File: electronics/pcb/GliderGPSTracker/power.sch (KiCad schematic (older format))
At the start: 28 parts

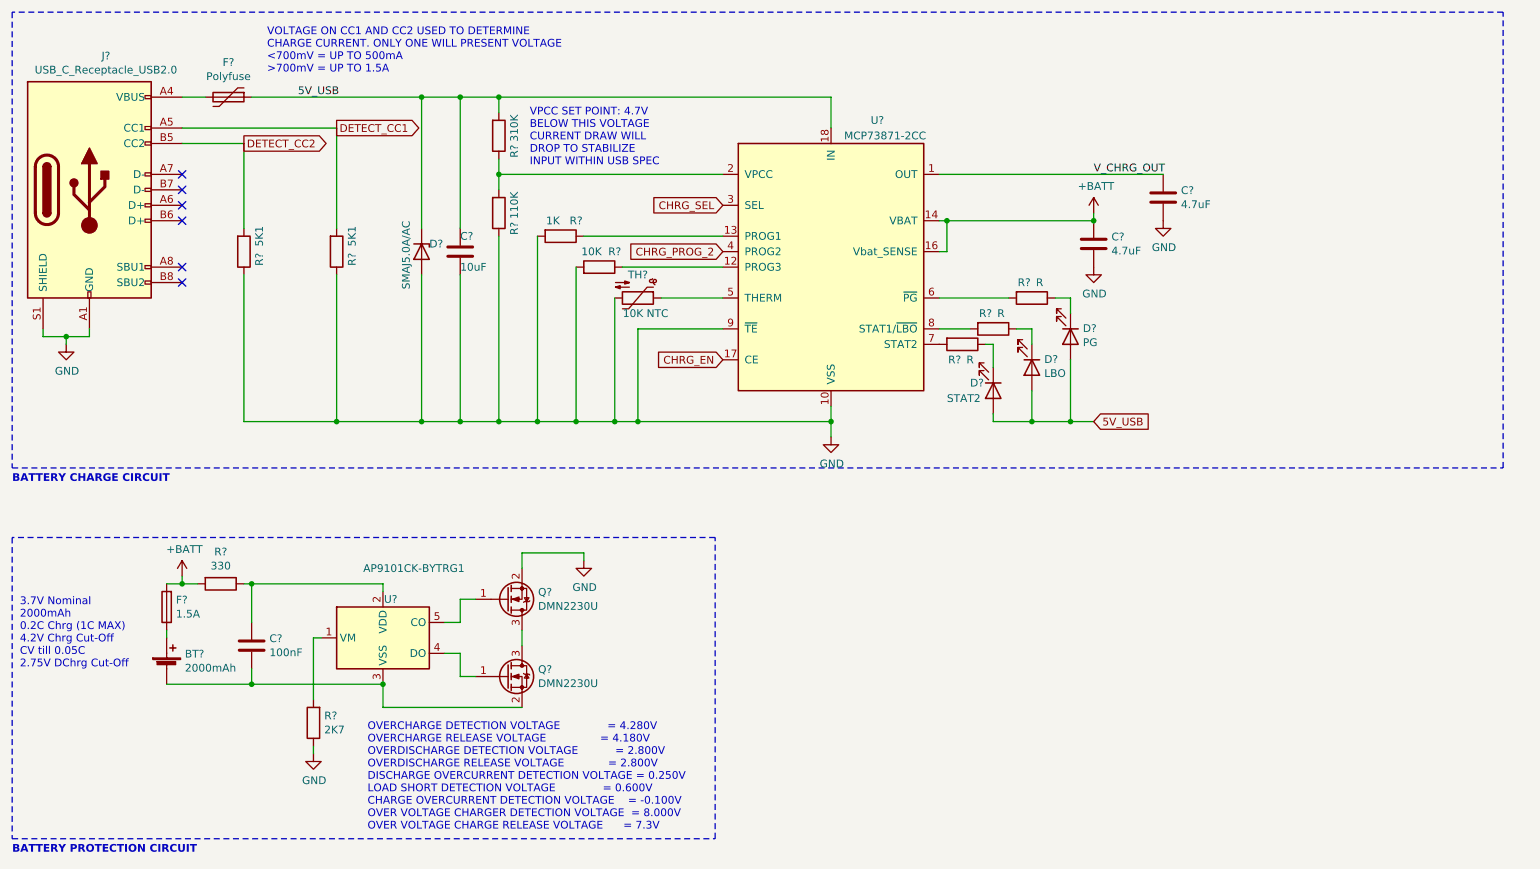
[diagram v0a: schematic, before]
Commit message: Task: Begin SIM7000E implementation
Work has begun on adding the SIM7000E module to the schematic.
A schematic symbol and footprint have been made to this end.
The basic SIM card circuit and power circuit has been set up
which include ESD protection IC's.
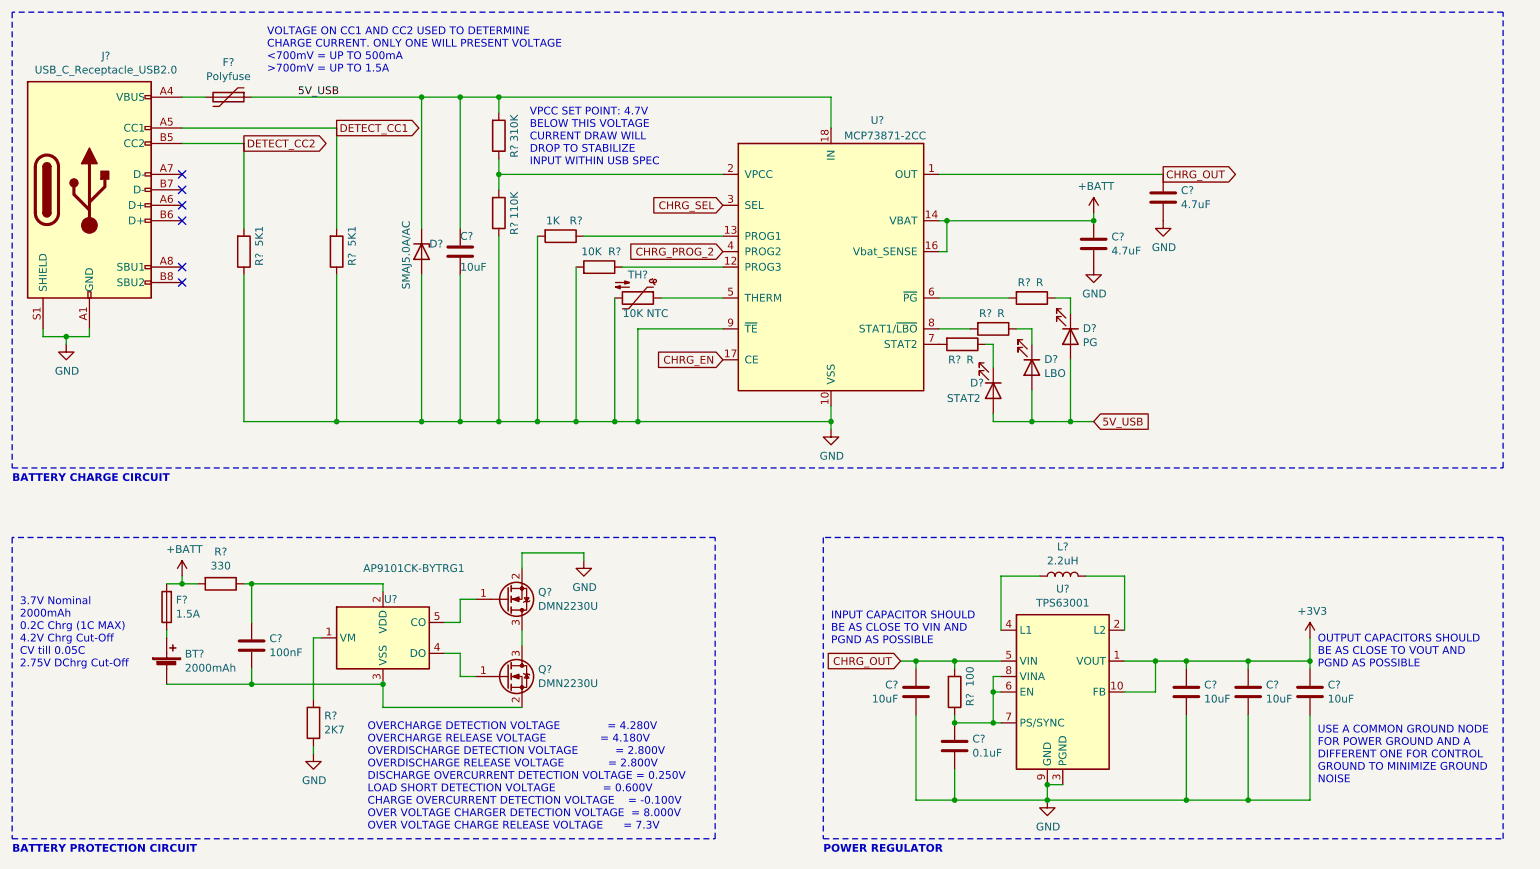
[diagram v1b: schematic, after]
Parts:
- added C? (x4): 10uF, symbol Device:C
- added C?: 0.1uF, symbol Device:C
- added L?: 2.2uH, symbol Device:L
- added R?: 100, symbol Device:R
- added U?: TPS63001, Package_SON:Texas_DRC0010J_ThermalVias, symbol Regulator_Switching:TPS63001
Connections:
- net GND: now also C?.2, C?.2, C?.2, C?.2, C?.2, U?.11 (PGND), U?.3 (PGND), U?.9 (GND)
- net V_CHRG_OUT renamed CHRG_OUT
- net CHRG_OUT: now also C?.1, R?.2, U?.5 (VIN)
- new net: L?.2, U?.2 (L2)
- new net: L?.1, U?.4 (L1)
- new net: C?.1, R?.1, U?.6 (EN), U?.7 (PS/SYNC), U?.8 (VINA)
- new net +3V3: C?.1, C?.1, C?.1, U?.1 (VOUT), U?.10 (FB)
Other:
- note added: "INPUT CAPACITOR SHOULD\nBE AS CLOSE TO VIN AND \nPGND AS POSSIBLE"
- note added: "OUTPUT CAPACITORS SHOULD\nBE AS CLOSE TO VOUT AND \nPGND AS POSSIBLE"
- note added: "POWER REGULATOR"
- note added: "USE A COMMON GROUND NODE\nFOR POWER GROUND AND A \nDIFFERENT ONE FOR CONTROL\nGROUND TO MINIMIZE GROUND\nNOISE"

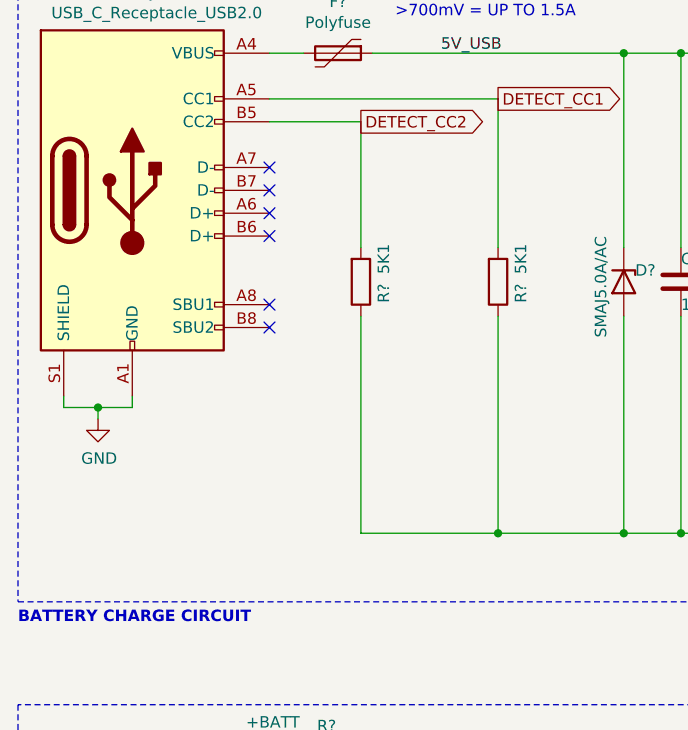
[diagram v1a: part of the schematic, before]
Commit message: Task: SIM7000 Powerkey, reset, USB, UART implementation
The SIM7000 schematic has been updated to include the recommended
layouts for the Powerkey pin, reset pin, USB and UART buses, and
netlight pin. The usb connector in the power schematic has also
been updated to accomodate the additions.
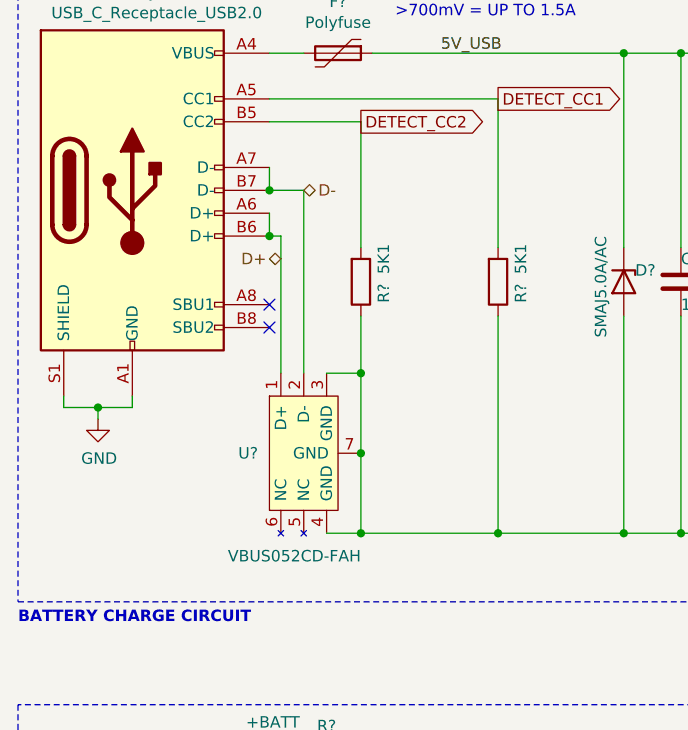
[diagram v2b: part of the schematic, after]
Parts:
- added U?: VBUS052CD-FAH, symbol GliderGPSLibrary:VBUS052CD-FAH
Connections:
- net GND: now also U?.3 (GND), U?.4 (GND), U?.7 (GND)
- net D+: now reaches J?.A6 (D+)
- net D+: now also J?.B6 (D+), U?.1 (D+)
- net D-: now reaches J?.A7 (D-)
- net D-: now also J?.B7 (D-), U?.2 (D-)
- no-connect marks 6 -> 2
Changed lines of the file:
@@
 $Descr A4 11693 8268
 encoding utf-8
-Sheet 2 3
+Sheet 2 4
 Title "POWER"
 Date ""
@@
 	1    0    0    -1
 $EndComp
-$Comp
-L Device:R R?
-U 1 1 6094CFBA
-P 2450 2400
-AR Path="/6094CFBA" Ref="R?"  Part="1"
-AR Path="/6090E0C9/6094CFBA" Ref="R?"  Part="1"
-F 0 "R?" V 2550 2450 50  0000 C CNN
-F 1 "5K1" V 2550 2300 50  0000 C CNN
-F 2 "" V 2380 2400 50  0001 C CNN
-F 3 "~" H 2450 2400 50  0001 C CNN
-	1    2450 2400
-	1    0    0    1
-$EndComp
 Wire Wire Line
 	2050 1700 2450 1700
-Wire Wire Line
-	2450 1700 2450 2250
-Wire Wire Line
-	2450 2550 2450 3500
-Wire Wire Line
-	2450 3500 3050 3500
 Connection ~ 3050 3500
 Text GLabel 2450 1700 2    50   Output ~ 0
@@
 NoConn ~ 2050 2500
 NoConn ~ 2050 2600
-NoConn ~ 2050 2200
-NoConn ~ 2050 2100
-NoConn ~ 2050 2000
-NoConn ~ 2050 1900
 Text Notes 2600 1250 0    50   ~ 0
 VOLTAGE ON CC1 AND CC2 USED TO DETERMINE\nCHARGE CURRENT. ONLY ONE WILL PRESENT VOLTAGE\n<700mV = UP TO 500mA\n>700mV = UP TO 1.5A
@@
 Text Notes 6200 6300 0    50   ~ 10
 POWER REGULATOR
+Wire Wire Line
+	2050 2100 2050 2200
+Connection ~ 2050 2200
+Wire Wire Line
+	2050 1900 2050 2000
+Connection ~ 2050 2000
+Wire Wire Line
+	2050 2200 2100 2200
+Wire Wire Line
+	2050 2000 2200 2000
+Wire Wire Line
+	2100 2200 2100 2800
+Wire Wire Line
+	2200 2000 2200 2800
+Connection ~ 2450 3500
+Wire Wire Line
+	2300 3500 2450 3500
+Wire Wire Line
+	2450 2800 2450 3150
+Wire Wire Line
+	2300 2800 2450 2800
+Wire Wire Line
+	2450 3150 2450 3500
+Connection ~ 2450 3150
+$Comp
+L GliderGPSLibrary:VBUS052CD-FAH U?
+U 1 1 60CF3EBE
+P 2200 3150
+F 0 "U?" V 2200 3350 50  0000 L CNN
+F 1 "VBUS052CD-FAH" V 2650 2900 50  0000 L CNN
+F 2 "" H 2200 2500 50  0001 C CNN
+F 3 "" H 2200 2500 50  0001 C CNN
+	1    2200 3150
+	0    -1   1    0
+$EndComp
+Wire Wire Line
+	2450 3500 3050 3500
+Connection ~ 2450 2800
+Wire Wire Line
+	2450 2550 2450 2800
+Wire Wire Line
+	2450 1700 2450 2250
+$Comp
+L Device:R R?
+U 1 1 6094CFBA
+P 2450 2400
+AR Path="/6094CFBA" Ref="R?"  Part="1"
+AR Path="/6090E0C9/6094CFBA" Ref="R?"  Part="1"
+F 0 "R?" V 2550 2450 50  0000 C CNN
+F 1 "5K1" V 2550 2300 50  0000 C CNN
+F 2 "" V 2380 2400 50  0001 C CNN
+F 3 "~" H 2450 2400 50  0001 C CNN
+	1    2450 2400
+	1    0    0    1
+$EndComp
+Text HLabel 2200 2000 2    50   BiDi ~ 0
+D-
+Text HLabel 2100 2300 0    50   BiDi ~ 0
+D+
 $EndSCHEMATC
